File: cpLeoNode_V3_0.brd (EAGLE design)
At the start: 83.5 x 68.6 mm, 46 parts, among them CON6 0.100, CON7 0.100, J1 0.100, J2 0.100, P1 CA CC, U1 MAX3465CPD, U2 NE555P

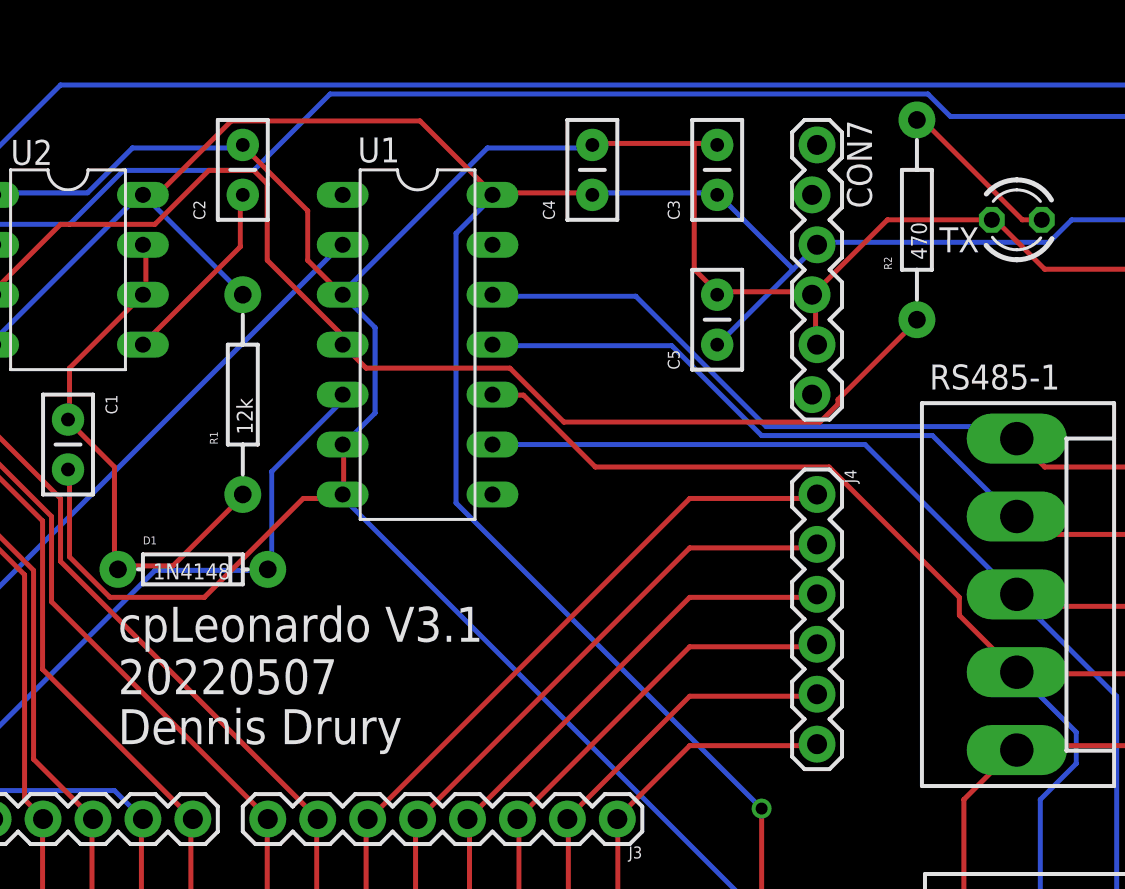
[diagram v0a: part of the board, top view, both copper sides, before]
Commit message: adjustments of Leonardo header to fit better
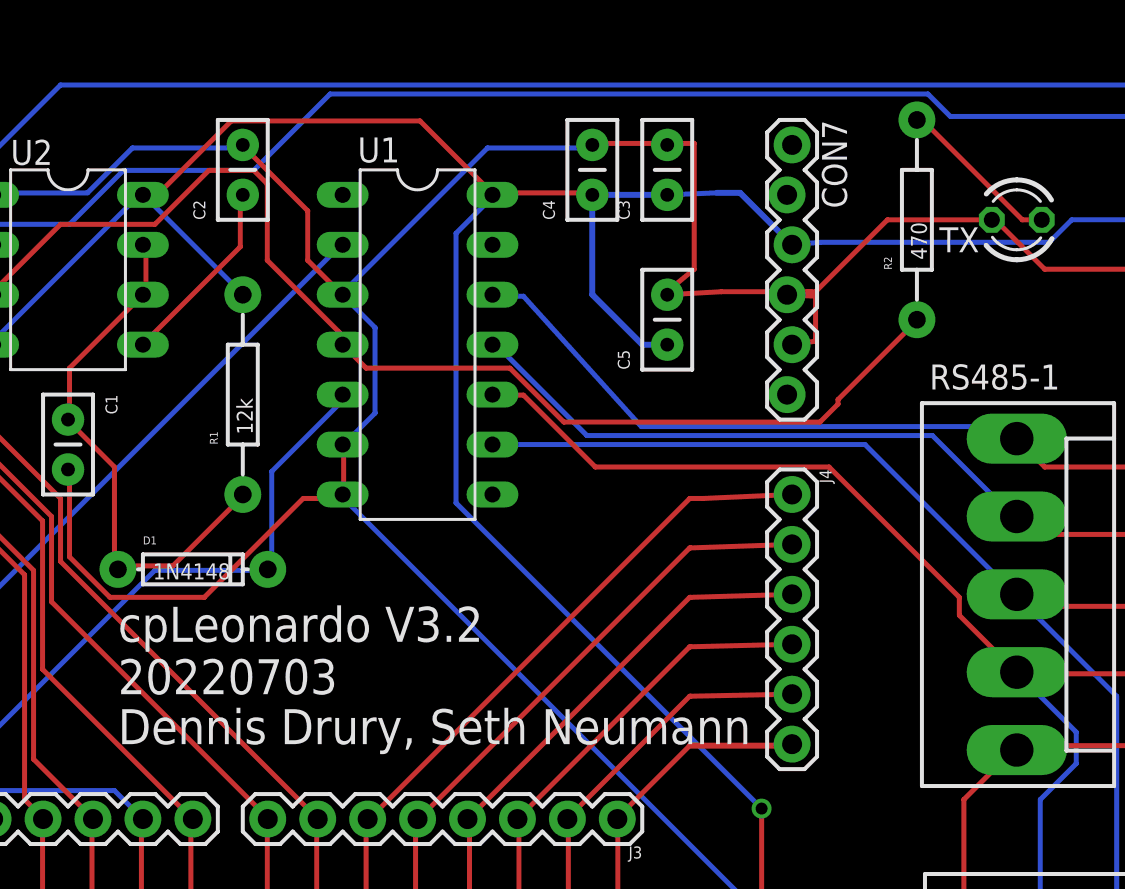
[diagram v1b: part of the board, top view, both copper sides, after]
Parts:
- moved C3 2.54 mm to (45.7, 59.7)
- moved C5 2.54 mm to (45.7, 52.1)
- moved CON7 1.27 mm to (52.1, 61.0)
- moved J4 1.27 mm to (52.1, 43.2)
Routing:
- net GND: track 180.4 -> 186.5 mm
- net VCC: track 135.8 -> 139.3 mm
- net A0: track 35.4 -> 34.0 mm
- net A1: track 31.8 -> 30.4 mm
- net A2: track 28.2 -> 26.8 mm
- net A3: track 24.6 -> 23.2 mm
- net A4: track 21.0 -> 19.6 mm
- net A5: track 17.4 -> 16.1 mm
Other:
- board text added: "Dennis Drury, Seth Neumann"
- board text added: "cpLeonardo V3.2 20220703"
- board text removed: "Dennis Drury"
- board text removed: "cpLeonardo V3.1 20220507"

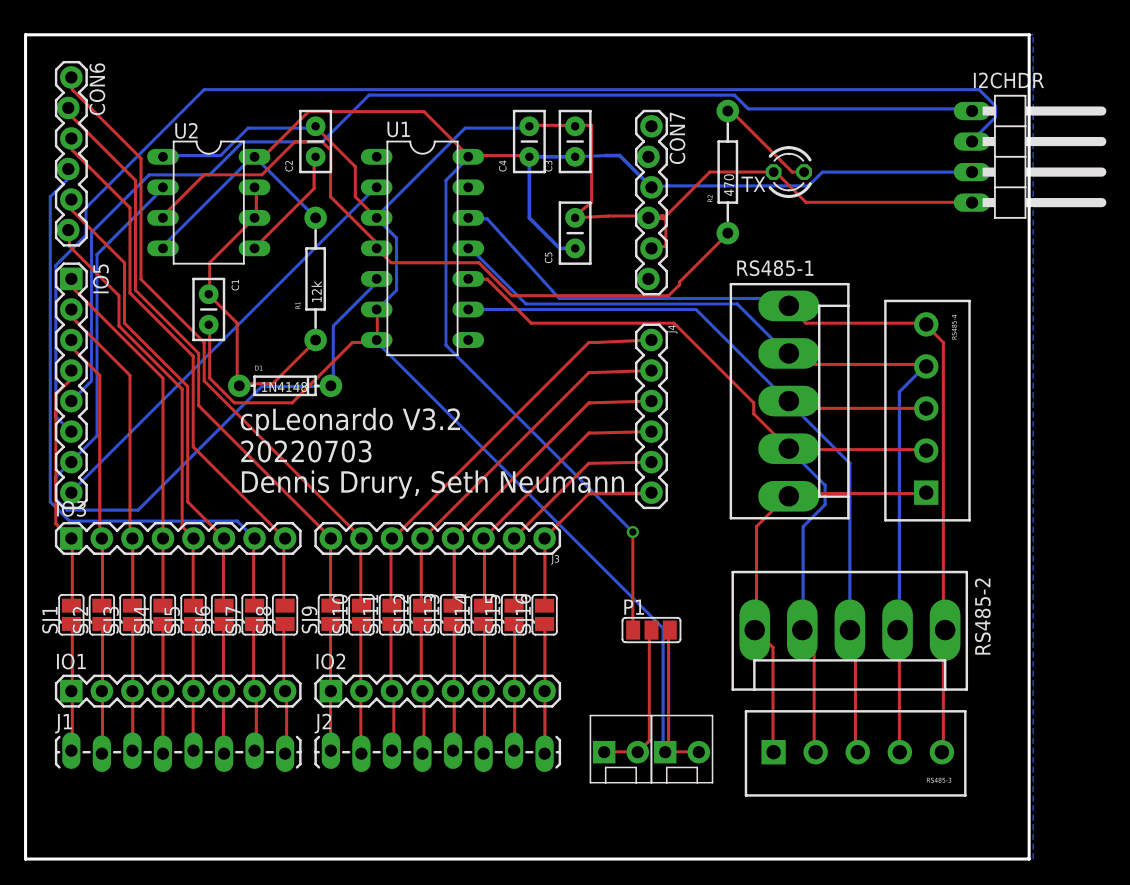
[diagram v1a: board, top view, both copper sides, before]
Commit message: A bunch of cleanup after moving things around
1 - move Arduino connectors closer together for better fit with the Leonardo
2 - added VCC plane and removed a lot of old VCC and GND traces
3- added labels on top to help orient Leonardo
4 - mirrored bottom labels and moved to bplace for readability
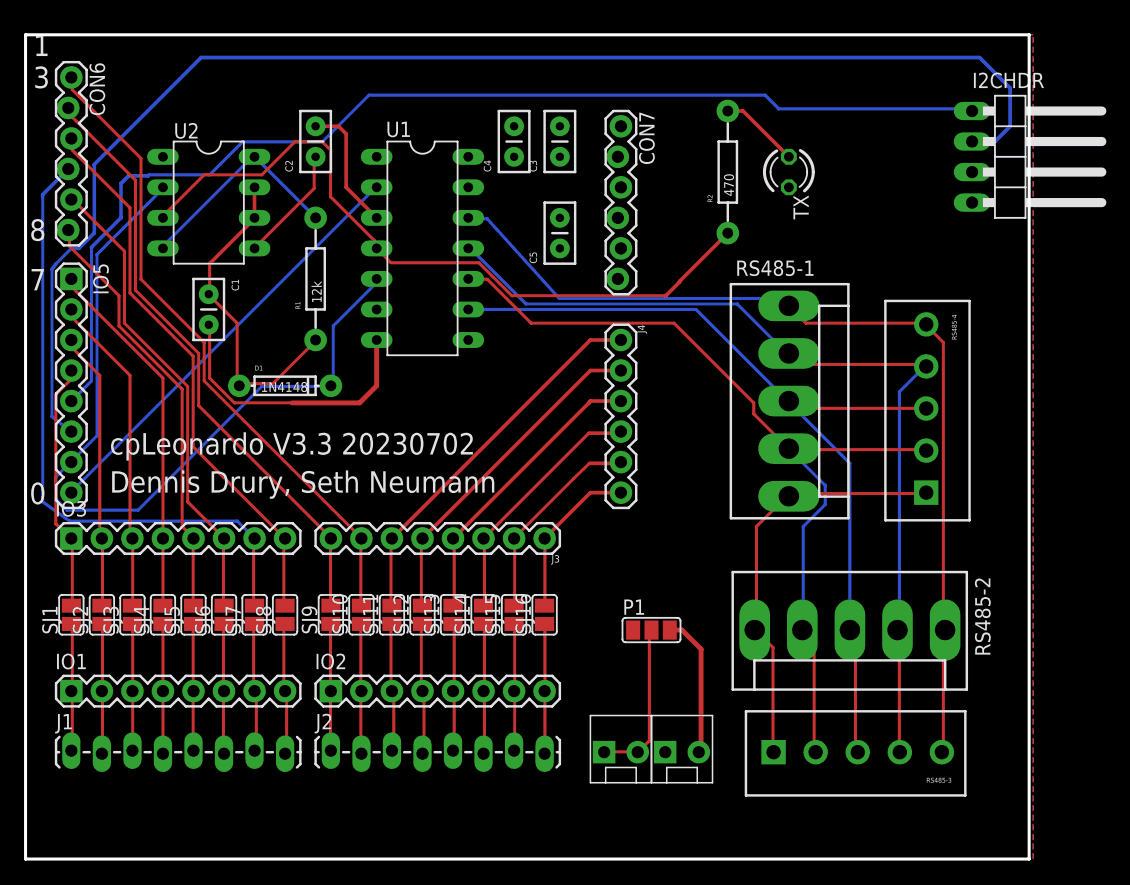
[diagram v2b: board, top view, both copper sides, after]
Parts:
- added U$2: (no value), MRCSLogoBtm:MRCSLOGOBTM
- moved U$1 7.24 mm to (37.5, 33.7)
- moved CON7 2.54 mm to (49.5, 61.0)
- moved J4 2.54 mm to (49.5, 43.2)
- moved C3 1.27 mm to (44.5, 59.7)
- moved C4 1.27 mm to (40.6, 59.7)
- moved C5 1.27 mm to (44.5, 52.1)
- turned TX to 90 degrees
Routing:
- net GND: track 186.5 -> 46.5 mm
- net VCC: track 139.3 -> 18.3 mm, vias 1 -> 0
- net D2: track 104.3 -> 112.6 mm
- net A5: track 16.1 -> 13.5 mm
- net A4: track 19.6 -> 17.1 mm
- net A3: track 23.2 -> 20.7 mm
- net A1: track 30.4 -> 27.9 mm
- net A0: track 34.0 -> 31.5 mm
- net A2: track 26.8 -> 24.4 mm
- net N$29: track 8.63 -> 6.66 mm
- net D3: track 93.3 -> 94.2 mm
- net D10: track 52.2 -> 53.1 mm
- added copper zone on layer 1, net VCC
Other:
- board text added: "0"
- board text added: "1 3"
- board text added: "7"
- board text added: "8"
- board text added: "A5 A4 A3 A2 A1 A0 D13 D12"
- board text added: "D11 D10 D9 D8"
- board text added: "GND LED COM"
- board text added: "cpLeonardo V3.3 20230702"
- board text removed: "A0"
- board text removed: "A1"
- board text removed: "A2"
- board text removed: "A3"
- board text removed: "A4"
- board text removed: "A5"
- board text removed: "D10"
- board text removed: "D11"
- board text removed: "D12"
- board text removed: "D13"
- board text removed: "D8"
- board text removed: "D9"
- board text removed: "Gnd"
- board text removed: "LED Com"
- board text removed: "cpLeonardo V3.2 20220703"
